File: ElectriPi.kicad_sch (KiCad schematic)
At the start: 59 parts, among them IC2 TPS51397ARJER, J1 2444, J2 JST XH 01x02, J3 JST XH 01x02, J6 Raspberry_Pi_2_3, J8 JST XH 01x02, Q1 SiA471DJ, Q2 SiA430DJT, U1 LM74700

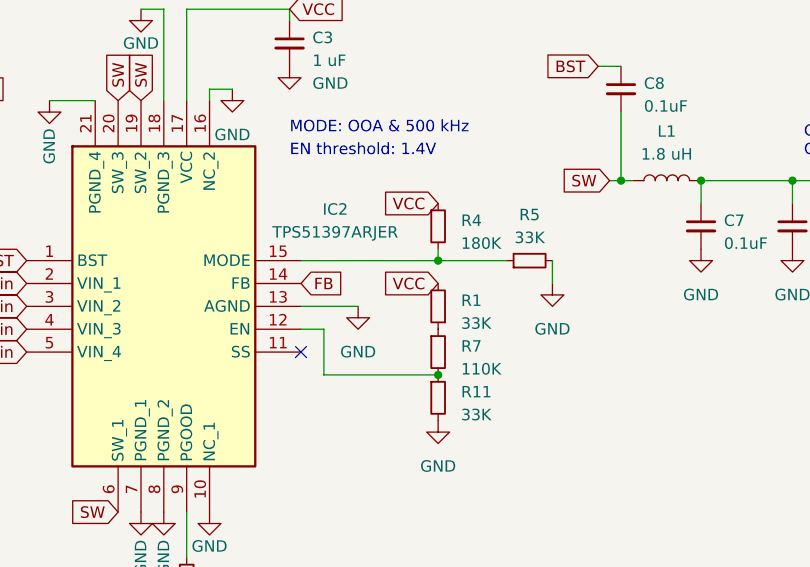
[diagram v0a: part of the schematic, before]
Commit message: First pass of layout complete
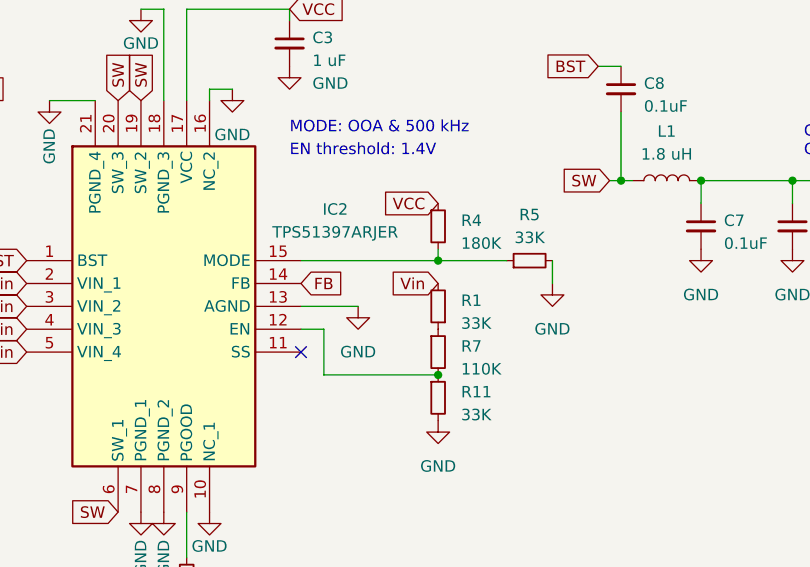
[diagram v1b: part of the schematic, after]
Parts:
- H5, H6, H7, H8: footprint MountingHole:MountingHole_3.5mm -> MountingHole:MountingHole_3.5mm_Pad
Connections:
- net VCC: no longer R1.2
- net Vin: now also R1.2
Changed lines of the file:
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@@
     )
   )
-  (global_label "VCC" (shape input) (at 151.13 62.23 180) (fields_autoplaced)
+  (global_label "Vin" (shape input) (at 151.13 62.23 180) (fields_autoplaced)
     (effects (font (size 1.27 1.27)) (justify right))
-    (property "Intersheetrefs" "${INTERSHEET_REFS}" (at 144.5956 62.23 0)
+    (property "Intersheetrefs" "${INTERSHEET_REFS}" (at 145.3818 62.23 0)
       (effects (font (size 1.27 1.27)) (justify right) hide)
     )
@@
       (effects (font (size 1.27 1.27)) (justify left))
     )
-    (property "Footprint" "MountingHole:MountingHole_3.5mm" (at 98.425 181.229 0)
+    (property "Footprint" "MountingHole:MountingHole_3.5mm_Pad" (at 98.425 181.229 0)
       (effects (font (size 1.27 1.27)) hide)
     )
@@
       (effects (font (size 1.27 1.27)) (justify left))
     )
-    (property "Footprint" "MountingHole:MountingHole_3.5mm" (at 98.425 172.085 0)
+    (property "Footprint" "MountingHole:MountingHole_3.5mm_Pad" (at 98.425 172.085 0)
       (effects (font (size 1.27 1.27)) hide)
     )
@@
       (effects (font (size 1.27 1.27)) (justify left))
     )
-    (property "Footprint" "MountingHole:MountingHole_3.5mm" (at 98.425 185.801 0)
+    (property "Footprint" "MountingHole:MountingHole_3.5mm_Pad" (at 98.425 185.801 0)
       (effects (font (size 1.27 1.27)) hide)
     )
@@
       (effects (font (size 1.27 1.27)) (justify left))
     )
-    (property "Footprint" "MountingHole:MountingHole_3.5mm" (at 98.425 176.657 0)
-      (effects (font (size 1.27 1.27)) hide)
-    )
+    (property "Footprint" "MountingHole:MountingHole_3.5mm_Pad" (at 98.425 176.657 0)
+      (effects (font (size 1.27 1.27)) hide)
+    )

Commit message: Added question to sch
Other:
- note added: "Should D4's NC pin be grounded?"
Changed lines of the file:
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@@
+    (effects (font (size 1.27 1.27)) (justify left bottom))
+  )
+  (text "Should D4's NC\npin be grounded?" (at 77.47 62.23 0)
     (effects (font (size 1.27 1.27)) (justify left bottom))
   )

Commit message: Changed to higher current inductor, which had larger footprint
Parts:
- L1: footprint Inductor_SMD:L_Bourns_SRP7028A_7.3x6.6mm -> Inductor_SMD:L_Vishay_IHLP-4040; LCSC (none) -> C506636; Mouser 652-SRP7028A-1R8M -> 70-IHLP4040DZER1R8M1
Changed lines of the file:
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@@
       (effects (font (size 1.27 1.27)))
     )
-    (property "Footprint" "Inductor_SMD:L_Bourns_SRP7028A_7.3x6.6mm" (at 176.53 50.8 0)
+    (property "Footprint" "Inductor_SMD:L_Vishay_IHLP-4040" (at 176.53 50.8 0)
       (effects (font (size 1.27 1.27)) hide)
     )
-    (property "Datasheet" "https://www.mouser.com/datasheet/2/54/srp7028a-1391359.pdf" (at 176.53 50.8 0)
+    (property "Datasheet" "https://www.vishay.com/docs/34192/lp40dz11.pdf" (at 176.53 50.8 0)
       (effects (font (size 1.27 1.27)) hide)
     )
-    (property "LCSC" "" (at 176.53 50.8 90)
+    (property "LCSC" "C506636" (at 176.53 50.8 90)
       (effects (font (size 1.27 1.27)) hide)
     )
@@
       (effects (font (size 1.27 1.27)) hide)
     )
-    (property "Mouser" "652-SRP7028A-1R8M" (at 176.53 50.8 90)
+    (property "Mouser" "70-IHLP4040DZER1R8M1" (at 176.53 50.8 90)
       (effects (font (size 1.27 1.27)) hide)
     )

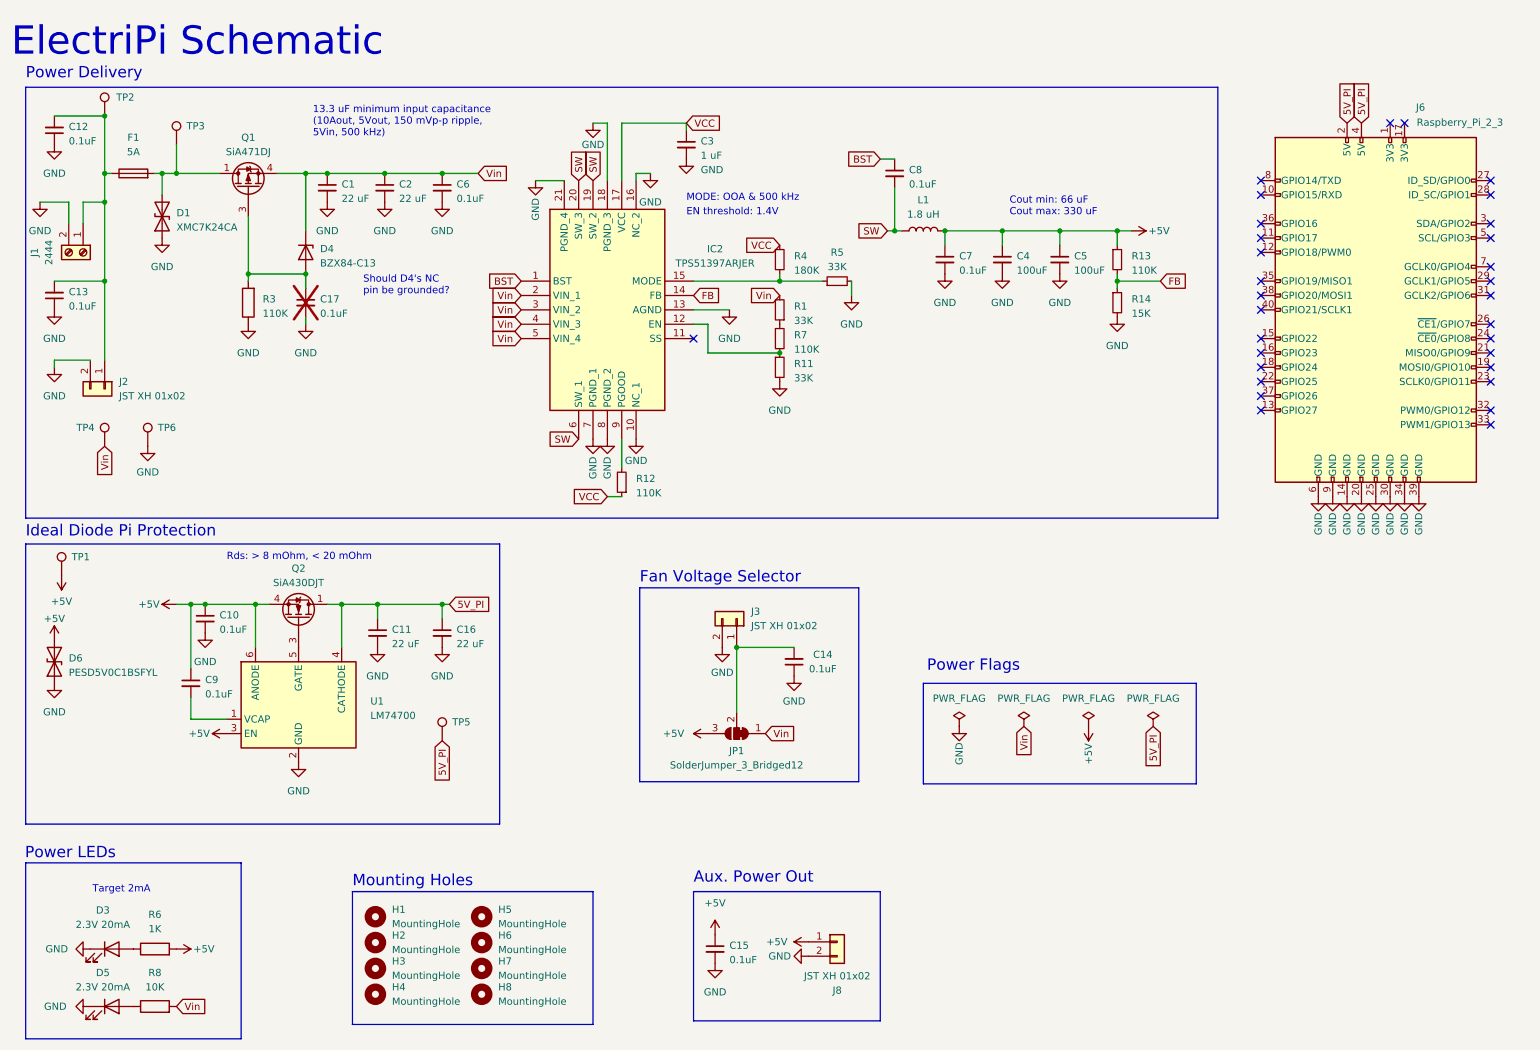
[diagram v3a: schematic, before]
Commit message: Add bulk capacitance and update cap size
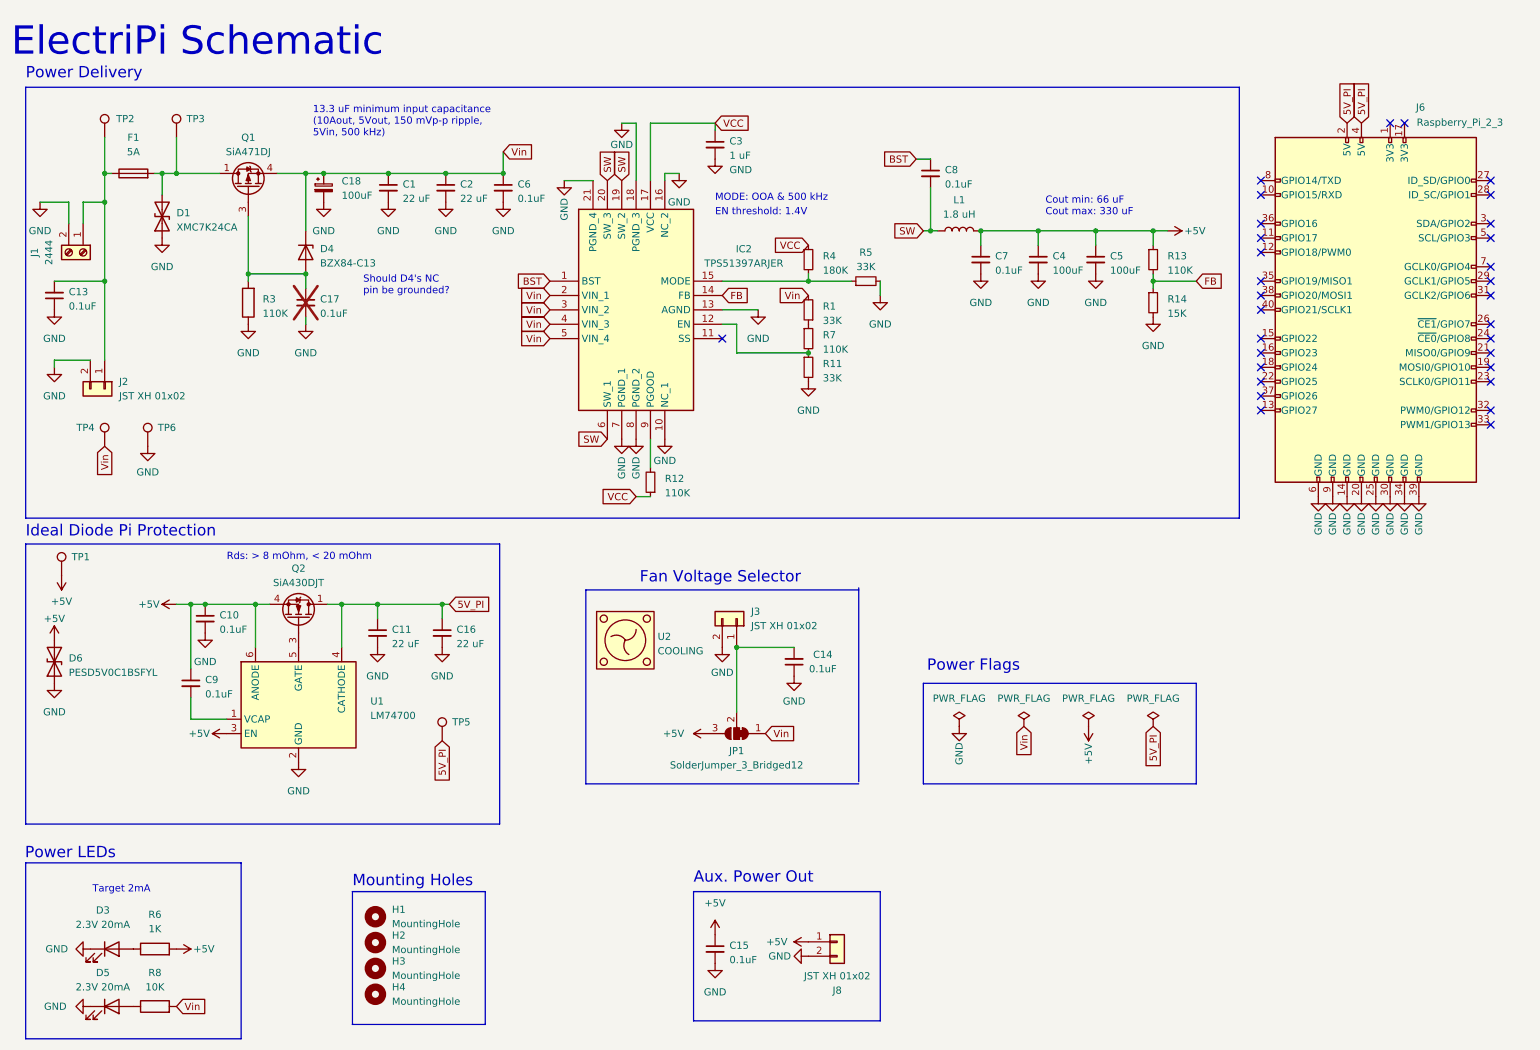
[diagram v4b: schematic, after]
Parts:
- removed C12: 0.1uF, Capacitor_SMD:C_0402_1005Metric, symbol Device:C_Small
- removed H5, H6, H7, H8: MountingHole, MountingHole:MountingHole_3.5mm_Pad, symbol Mechanical:MountingHole
- added C18: 100uF, Capacitor_SMD:CP_Elec_8x10, symbol Device:C_Polarized_Small
- added U2: COOLING, FAN:4040, symbol FAN:COOLING
- C1, C2: footprint Capacitor_SMD:C_0805_2012Metric -> Capacitor_SMD:C_2220_5650Metric_Pad1.97x5.40mm_HandSolder; Mouser (none) -> 810-C5750X7S2A226280
- C10, C13, C14, C15, C17, C6, C7, C8, C9: Mouser (none) -> 81-GRM155R62A104KE4J
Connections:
- net GND: now also C18.2
- net Vin: now also C18.1
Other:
- moved on the sheet: C1, C2, C3, C4, C5, C6, C7, C8, IC2, L1, R1, R11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

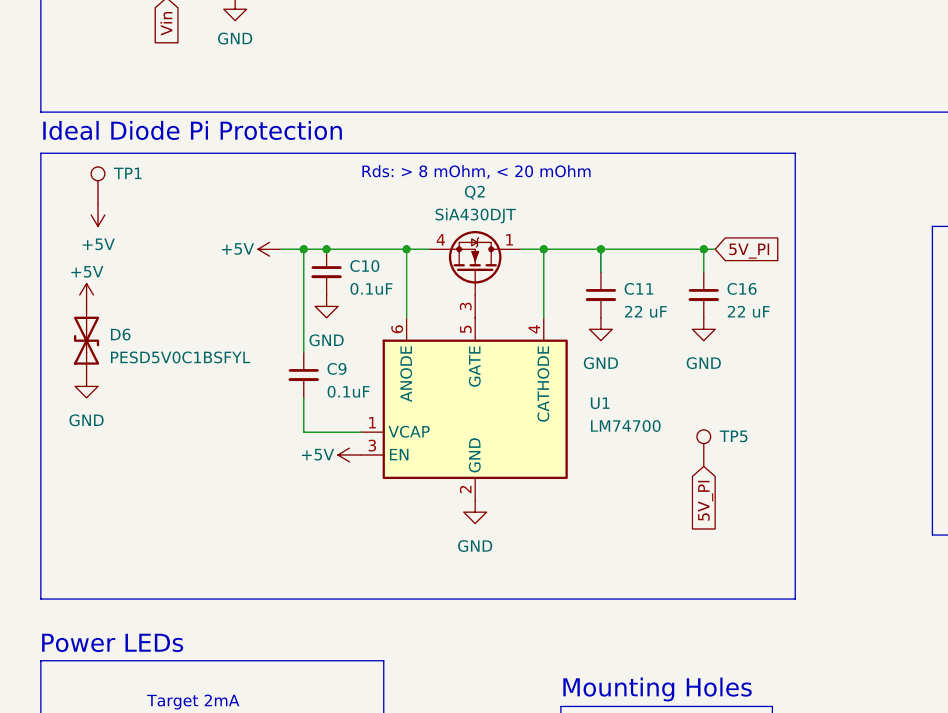
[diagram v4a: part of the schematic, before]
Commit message: update holdup capacitance
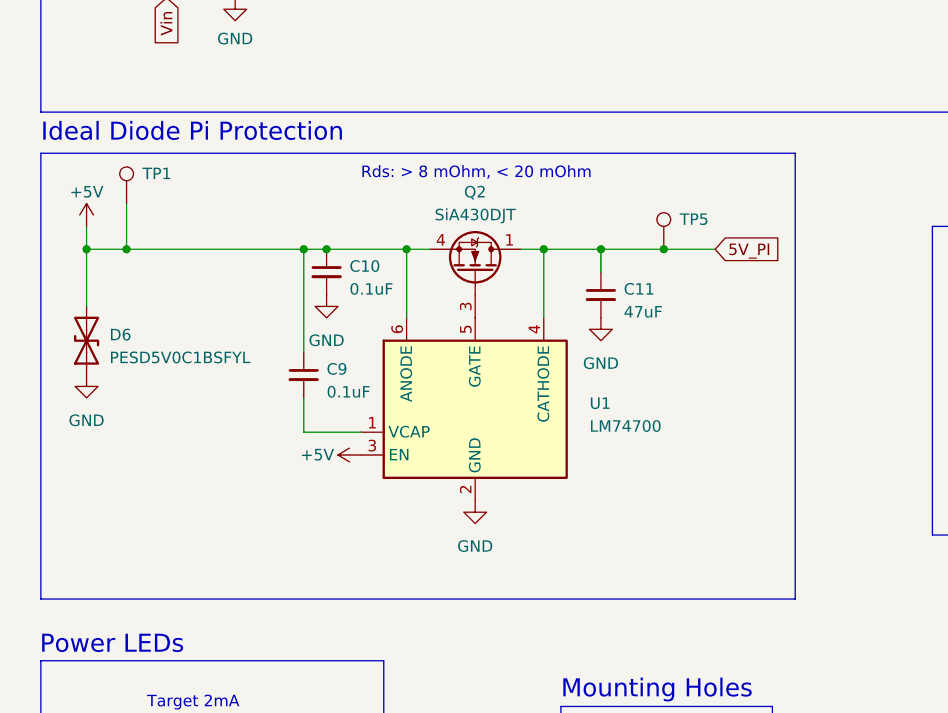
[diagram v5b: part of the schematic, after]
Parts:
- removed C16: 22 uF, Capacitor_SMD:C_0805_2012Metric, symbol Device:C_Small
- C11: value 22 uF -> 47uF; Mouser (none) -> 81-GRM21BR61A476ME5L
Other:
- moved on the sheet: TP1
